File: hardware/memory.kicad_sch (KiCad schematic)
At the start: 5 parts, among them U2 ICE40HX4K-TQ144

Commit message: Add 3d models, re-place exp slots, add components
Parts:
- added U3, U4: SN74ALVC164245, Package_SO:TSSOP-48_6.1x12.5mm_P0.5mm, symbol 68040:SN74ALVC164245
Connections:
- net D0: now also U3.2 (1B1); no longer J10.2 (DQ0), J11.2 (DQ0), J12.2 (DQ0), J9.2 (DQ0)
- net D1: now also U3.3 (1B2); no longer J10.4 (DQ1), J11.4 (DQ1), J12.4 (DQ1), J9.4 (DQ1)
- net D10: now also U3.16 (2B3); no longer J10.53 (DQ10), J11.53 (DQ10), J12.53 (DQ10), J9.53 (DQ10)
- net D11: now also U3.17 (2B4); no longer J10.55 (DQ11), J11.55 (DQ11), J12.55 (DQ11), J9.55 (DQ11)
- net D12: now also U3.19 (2B5); no longer J10.57 (DQ12), J11.57 (DQ12), J12.57 (DQ12), J9.57 (DQ12)
- net D13: now also U3.20 (2B6); no longer J10.61 (DQ13), J11.61 (DQ13), J12.61 (DQ13), J9.61 (DQ13)
- net D14: now also U3.22 (2B7); no longer J10.63 (DQ14), J11.63 (DQ14), J12.63 (DQ14), J9.63 (DQ14)
- net D15: now also U3.23 (2B8); no longer J10.65 (DQ15), J11.65 (DQ15), J12.65 (DQ15), J9.65 (DQ15)
- net D16: now also U4.2 (1B1); no longer J10.3 (DQ16), J11.3 (DQ16), J12.3 (DQ16), J9.3 (DQ16)
- net D17: now also U4.3 (1B2); no longer J10.5 (DQ17), J11.5 (DQ17), J12.5 (DQ17), J9.5 (DQ17)
- net D18: now also U4.5 (1B3); no longer J10.7 (DQ18), J11.7 (DQ18), J12.7 (DQ18), J9.7 (DQ18)
- net D19: now also U4.6 (1B4); no longer J10.9 (DQ19), J11.9 (DQ19), J12.9 (DQ19), J9.9 (DQ19)
- net D2: now also U3.5 (1B3); no longer J10.6 (DQ2), J11.6 (DQ2), J12.6 (DQ2), J9.6 (DQ2)
- net D20: now also U4.8 (1B5); no longer J10.21 (DQ20), J11.21 (DQ20), J12.21 (DQ20), J9.21 (DQ20)
- net D21: now also U4.9 (1B6); no longer J10.23 (DQ21), J11.23 (DQ21), J12.23 (DQ21), J9.23 (DQ21)
- net D22: now also U4.11 (1B7); no longer J10.25 (DQ22), J11.25 (DQ22), J12.25 (DQ22), J9.25 (DQ22)
- net D23: now also U4.12 (1B8); no longer J10.27 (DQ23), J11.27 (DQ23), J12.27 (DQ23), J9.27 (DQ23)
- net D24: now also U4.13 (2B1); no longer J10.50 (DQ24), J11.50 (DQ24), J12.50 (DQ24), J9.50 (DQ24)
- net D25: now also U4.14 (2B2); no longer J10.52 (DQ25), J11.52 (DQ25), J12.52 (DQ25), J9.52 (DQ25)
- net D26: now also U4.16 (2B3); no longer J10.54 (DQ26), J11.54 (DQ26), J12.54 (DQ26), J9.54 (DQ26)
- net D27: now also U4.17 (2B4); no longer J10.56 (DQ27), J11.56 (DQ27), J12.56 (DQ27), J9.56 (DQ27)
- net D28: now also U4.19 (2B5); no longer J10.58 (DQ28), J11.58 (DQ28), J12.58 (DQ28), J9.58 (DQ28)
- net D29: now also U4.20 (2B6); no longer J10.60 (DQ29), J11.60 (DQ29), J12.60 (DQ29), J9.60 (DQ29)
- net D3: now also U3.6 (1B4); no longer J10.8 (DQ3), J11.8 (DQ3), J12.8 (DQ3), J9.8 (DQ3)
- net D30: now also U4.22 (2B7); no longer J10.62 (DQ30), J11.62 (DQ30), J12.62 (DQ30), J9.62 (DQ30)
- net D31: now also U4.23 (2B8); no longer J10.64 (DQ31), J11.64 (DQ31), J12.64 (DQ31), J9.64 (DQ31)
- net D4: now also U3.8 (1B5); no longer J10.20 (DQ4), J11.20 (DQ4), J12.20 (DQ4), J9.20 (DQ4)
- net D5: now also U3.9 (1B6); no longer J10.22 (DQ5), J11.22 (DQ5), J12.22 (DQ5), J9.22 (DQ5)
- net D6: now also U3.11 (1B7); no longer J10.24 (DQ6), J11.24 (DQ6), J12.24 (DQ6), J9.24 (DQ6)
- net D7: now also U3.12 (1B8); no longer J10.26 (DQ7), J11.26 (DQ7), J12.26 (DQ7), J9.26 (DQ7)
- net D8: now also U3.13 (2B1); no longer J10.49 (DQ8), J11.49 (DQ8), J12.49 (DQ8), J9.49 (DQ8)
- net D9: now also U3.14 (2B2); no longer J10.51 (DQ9), J11.51 (DQ9), J12.51 (DQ9), J9.51 (DQ9)
- new net DRAM_D0: J10.2 (DQ0), J11.2 (DQ0), J12.2 (DQ0), J9.2 (DQ0), U3.47 (1A1)
- new net DRAM_D1: J10.4 (DQ1), J11.4 (DQ1), J12.4 (DQ1), J9.4 (DQ1), U3.46 (1A2)
- new net DRAM_D10: J10.53 (DQ10), J11.53 (DQ10), J12.53 (DQ10), J9.53 (DQ10), U3.33 (2A3)
- new net DRAM_D11: J10.55 (DQ11), J11.55 (DQ11), J12.55 (DQ11), J9.55 (DQ11), U3.32 (2A4)
- new net DRAM_D12: J10.57 (DQ12), J11.57 (DQ12), J12.57 (DQ12), J9.57 (DQ12), U3.30 (2A5)
- new net DRAM_D13: J10.61 (DQ13), J11.61 (DQ13), J12.61 (DQ13), J9.61 (DQ13), U3.29 (2A6)
- new net DRAM_D14: J10.63 (DQ14), J11.63 (DQ14), J12.63 (DQ14), J9.63 (DQ14), U3.27 (2A7)
- new net DRAM_D15: J10.65 (DQ15), J11.65 (DQ15), J12.65 (DQ15), J9.65 (DQ15), U3.26 (2A8)
- new net DRAM_D16: J10.3 (DQ16), J11.3 (DQ16), J12.3 (DQ16), J9.3 (DQ16), U4.47 (1A1)
- new net DRAM_D17: J10.5 (DQ17), J11.5 (DQ17), J12.5 (DQ17), J9.5 (DQ17), U4.46 (1A2)
- new net DRAM_D18: J10.7 (DQ18), J11.7 (DQ18), J12.7 (DQ18), J9.7 (DQ18), U4.44 (1A3)
- new net DRAM_D19: J10.9 (DQ19), J11.9 (DQ19), J12.9 (DQ19), J9.9 (DQ19), U4.43 (1A4)
- new net DRAM_D2: J10.6 (DQ2), J11.6 (DQ2), J12.6 (DQ2), J9.6 (DQ2), U3.44 (1A3)
- new net DRAM_D20: J10.21 (DQ20), J11.21 (DQ20), J12.21 (DQ20), J9.21 (DQ20), U4.41 (1A5)
- new net DRAM_D21: J10.23 (DQ21), J11.23 (DQ21), J12.23 (DQ21), J9.23 (DQ21), U4.40 (1A6)
- new net DRAM_D22: J10.25 (DQ22), J11.25 (DQ22), J12.25 (DQ22), J9.25 (DQ22), U4.38 (1A7)
- new net DRAM_D23: J10.27 (DQ23), J11.27 (DQ23), J12.27 (DQ23), J9.27 (DQ23), U4.37 (1A8)
- new net DRAM_D24: J10.50 (DQ24), J11.50 (DQ24), J12.50 (DQ24), J9.50 (DQ24), U4.36 (2A1)
- new net DRAM_D25: J10.52 (DQ25), J11.52 (DQ25), J12.52 (DQ25), J9.52 (DQ25), U4.35 (2A2)
- new net DRAM_D26: J10.54 (DQ26), J11.54 (DQ26), J12.54 (DQ26), J9.54 (DQ26), U4.33 (2A3)
- new net DRAM_D27: J10.56 (DQ27), J11.56 (DQ27), J12.56 (DQ27), J9.56 (DQ27), U4.32 (2A4)
- new net DRAM_D28: J10.58 (DQ28), J11.58 (DQ28), J12.58 (DQ28), J9.58 (DQ28), U4.30 (2A5)
- new net DRAM_D29: J10.60 (DQ29), J11.60 (DQ29), J12.60 (DQ29), J9.60 (DQ29), U4.29 (2A6)
- new net DRAM_D3: J10.8 (DQ3), J11.8 (DQ3), J12.8 (DQ3), J9.8 (DQ3), U3.43 (1A4)
- new net DRAM_D30: J10.62 (DQ30), J11.62 (DQ30), J12.62 (DQ30), J9.62 (DQ30), U4.27 (2A7)
- new net DRAM_D31: J10.64 (DQ31), J11.64 (DQ31), J12.64 (DQ31), J9.64 (DQ31), U4.26 (2A8)
- new net DRAM_D4: J10.20 (DQ4), J11.20 (DQ4), J12.20 (DQ4), J9.20 (DQ4), U3.41 (1A5)
- new net DRAM_D5: J10.22 (DQ5), J11.22 (DQ5), J12.22 (DQ5), J9.22 (DQ5), U3.40 (1A6)
- new net DRAM_D6: J10.24 (DQ6), J11.24 (DQ6), J12.24 (DQ6), J9.24 (DQ6), U3.38 (1A7)
- new net DRAM_D7: J10.26 (DQ7), J11.26 (DQ7), J12.26 (DQ7), J9.26 (DQ7), U3.37 (1A8)
- new net DRAM_D8: J10.49 (DQ8), J11.49 (DQ8), J12.49 (DQ8), J9.49 (DQ8), U3.36 (2A1)
- new net DRAM_D9: J10.51 (DQ9), J11.51 (DQ9), J12.51 (DQ9), J9.51 (DQ9), U3.35 (2A2)
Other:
- moved on the sheet: J10, J11, J12, J9, U2A, U2B, U2C, U2D, U2E

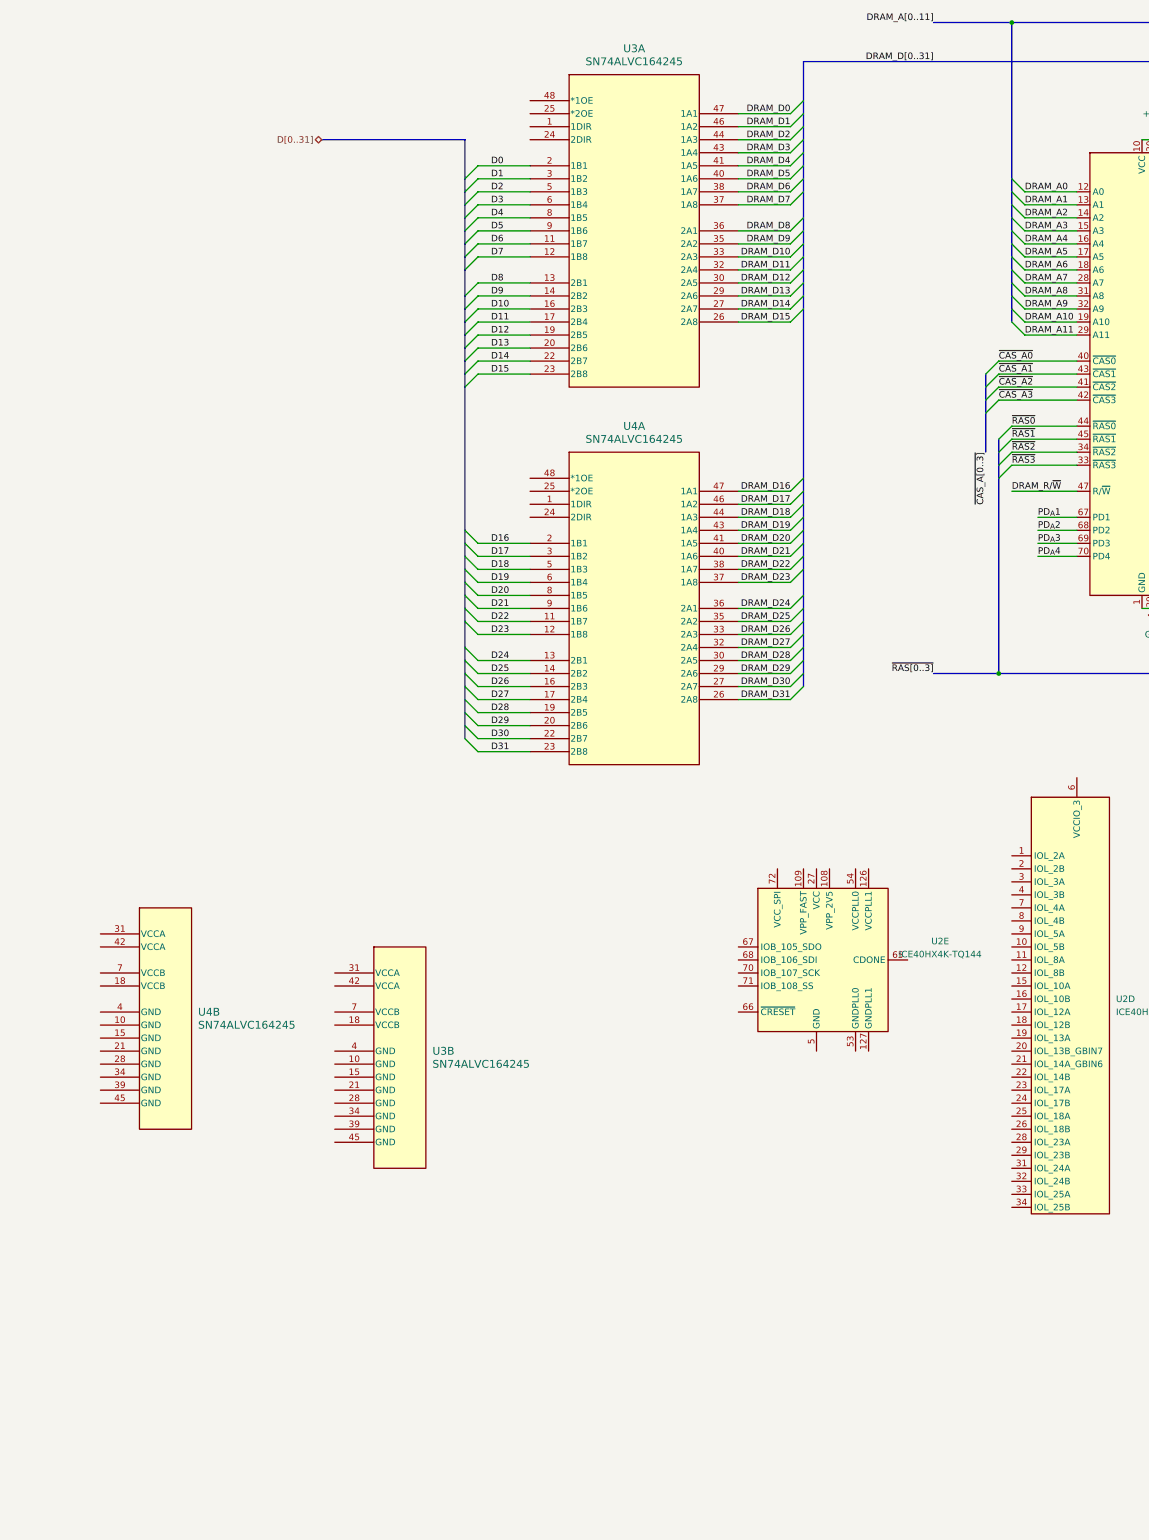
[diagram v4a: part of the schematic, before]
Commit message: reconfigure expansion slot schematic
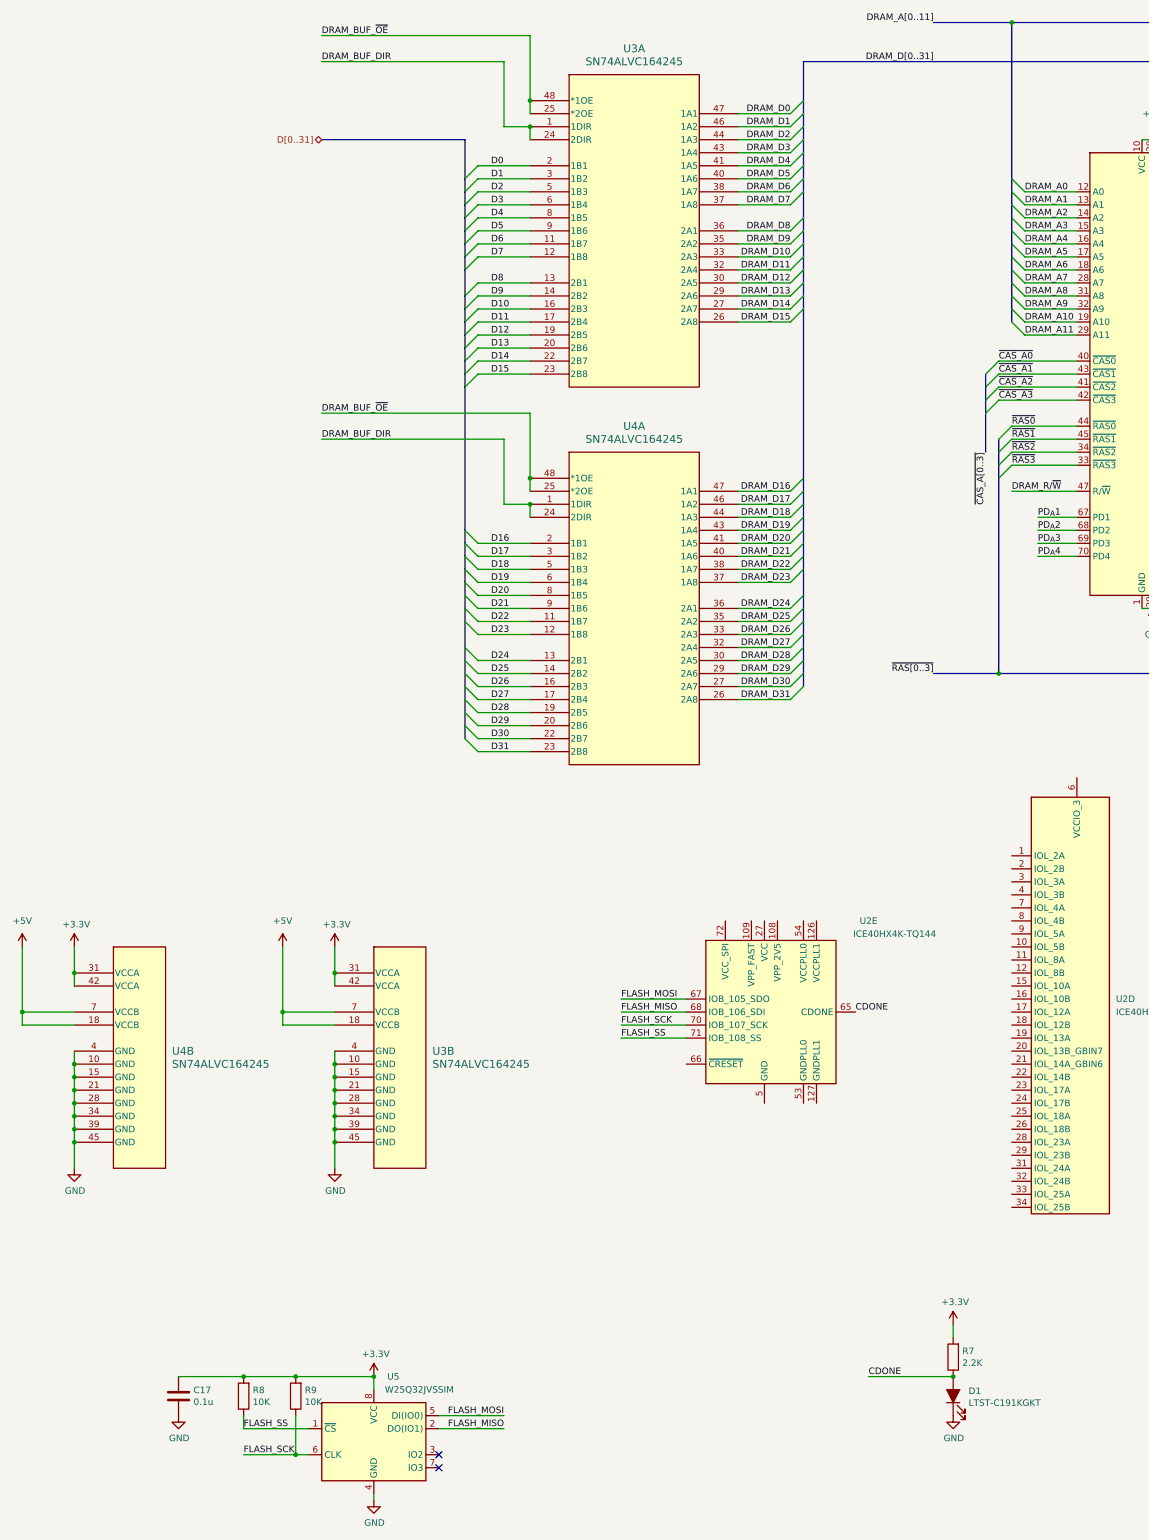
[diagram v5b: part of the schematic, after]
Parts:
- added C17: 0.1u, Capacitor_SMD:C_0603_1608Metric, symbol UPduino_v3.0:Device_C
- added D1: LTST-C191KGKT, LED_SMD:LED_0603_1608Metric, symbol UPduino_v3.0:Device_LED_ALT
- added R7: 2.2K, Resistor_SMD:R_0603_1608Metric, symbol UPduino_v3.0:Device_R
- added R8, R9: 10K, Resistor_SMD:R_0603_1608Metric, symbol UPduino_v3.0:Device_R
- added U5: W25Q32JVSSIM, Package_SO:SOIC-8_5.23x5.23mm_P1.27mm, symbol UPduino_v3.0:W25Q32JVSS-Memory_Flash
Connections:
- net +3V3: now also U3.31 (VCCA), U3.42 (VCCA), U4.31 (VCCA), U4.42 (VCCA), C17.1, R7.2, R8.2, R9.2, U5.8 (VCC)
- net GND: now also U3.10 (GND), U3.15 (GND), U3.21 (GND), U3.28 (GND), U3.34 (GND), U3.39 (GND), U3.4 (GND), U3.45 (GND), U4.10 (GND), U4.15 (GND), U4.21 (GND), U4.28 (GND), U4.34 (GND), U4.39 (GND), U4.4 (GND), U4.45 (GND), C17.2, D1.1 (K), U5.4 (GND)
- net DRAM_BUF_DIR: now reaches U4.1 (1DIR)
- net DRAM_BUF_DIR: now also U3.1 (1DIR), U3.24 (2DIR), U4.24 (2DIR)
- net DRAM_BUF_~{OE}: now reaches U4.25 (*2OE)
- net DRAM_BUF_~{OE}: now also U3.25 (*2OE), U3.48 (*1OE), U4.48 (*1OE)
- net CDONE: now reaches U2.65 (CDONE)
- net CDONE: now also D1.2 (A), R7.1
- net FLASH_MOSI: now reaches U2.67 (IOB_105_SDO)
- net FLASH_MOSI: now also U5.5 (DI(IO0))
- net FLASH_MISO: now reaches U2.68 (IOB_106_SDI)
- net FLASH_MISO: now also U5.2 (DO(IO1))
- net FLASH_SCK: now reaches U2.70 (IOB_107_SCK)
- net FLASH_SCK: now also R9.1, U5.6 (CLK)
- net FLASH_SS: now reaches U2.71 (IOB_108_SS)
- net FLASH_SS: now also R8.1, U5.1 (~{CS})
- net +5V: now reaches U3.18 (VCCB)
- net +5V: now also U3.7 (VCCB), U4.18 (VCCB), U4.7 (VCCB)
- no-connect marks 0 -> 2
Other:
- moved on the sheet: U2E, U4B

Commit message: updates
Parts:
- added RN3, RN4, RN5, RN6: 10k, Resistor_THT:R_Array_SIP5, symbol Device:R_Network04_US
- added U10, U9: 74HC165, Package_SO:SOIC-16_3.9x9.9mm_P1.27mm, symbol 74xx:74HC165
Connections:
- net +3V3: now also RN3.1 (common), RN4.1 (common), RN5.1 (common), U10.16 (VCC), U9.16 (VCC)
- net GND: now also U10.15 (~{CE}), U10.8 (GND), U9.10 (DS), U9.15 (~{CE}), U9.8 (GND)
- net PD_{A}1: now also RN5.2 (R1), U9.11 (D0)
- net PD_{A}2: now also RN5.3 (R2), U9.12 (D1)
- net PD_{A}3: now also RN5.4 (R3), U9.13 (D2)
- net PD_{A}4: now also RN5.5 (R4), U9.14 (D3)
- net PD_{B}1: now also RN6.2 (R1), U9.3 (D4)
- net PD_{B}2: now also RN6.3 (R2), U9.4 (D5)
- net PD_{B}3: now also RN6.4 (R3), U9.5 (D6)
- net PD_{B}4: now also RN6.5 (R4), U9.6 (D7)
- net PD_{C}1: now also RN3.2 (R1), U10.11 (D0)
- net PD_{C}2: now also RN3.3 (R2), U10.12 (D1)
- net PD_{C}3: now also RN3.4 (R3), U10.13 (D2)
- net PD_{C}4: now also RN3.5 (R4), U10.14 (D3)
- net PD_{D}1: now also RN4.2 (R1), U10.3 (D4)
- net PD_{D}2: now also RN4.3 (R2), U10.4 (D5)
- net PD_{D}3: now also RN4.4 (R3), U10.5 (D6)
- net PD_{D}4: now also RN4.5 (R4), U10.6 (D7)
- new net: U10.10 (DS), U9.9 (Q7)
- new net RAMPDSR_CLK: U10.2 (CP), U9.2 (CP)
- new net RAMPDSR_D_{OUT}: U10.9 (Q7)
- new net RAMPDSR_SH/~{LD}: U10.1 (~{PL}), U9.1 (~{PL})
- no-connect marks 2 -> 4
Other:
- note added: "Presence detect circuitry Should probably be HCT"

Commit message: updates
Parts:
- added U15, U16, U17, U18: SN74ALVC164245, Package_SO:TSSOP-48_6.1x12.5mm_P0.5mm, symbol 68040:SN74ALVC164245
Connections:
- net A0: now also U15.2 (1B1); no longer U2.88 (IOR_137)
- net A1: now also U15.3 (1B2); no longer U2.90 (IOR_138)
- net A10: now also U15.16 (2B3); no longer U2.101 (IOR_160)
- net A11: now also U15.17 (2B4); no longer U2.102 (IOR_161)
- net A12: now also U15.19 (2B5); no longer U2.104 (IOR_164)
- net A13: now also U15.20 (2B6); no longer U2.105 (IOR_165)
- net A14: now also U15.22 (2B7); no longer U2.106 (IOR_166)
- net A15: now also U15.23 (2B8); no longer U2.107 (IOR_167)
- net A16: now also U16.23 (2B8); no longer U2.110 (IOT_168)
- net A17: now also U16.22 (2B7); no longer U2.112 (IOT_169)
- net A18: now also U16.20 (2B6); no longer U2.113 (IOT_170)
- net A19: now also U16.19 (2B5); no longer U2.114 (IOT_171)
- net A2: now also U15.5 (1B3); no longer U2.91 (IOR_139)
- net A20: now also U16.17 (2B4); no longer U2.115 (IOT_172)
- net A21: now also U16.16 (2B3); no longer U2.116 (IOT_173)
- net A22: now also U16.14 (2B2); no longer U2.117 (IOT_174)
- net A23: now also U16.13 (2B1); no longer U2.118 (IOT_177)
- net A24: now also U16.12 (1B8); no longer U2.119 (IOT_178)
- net A25: now also U16.11 (1B7); no longer U2.120 (IOT_179)
- net A26: now also U16.9 (1B6); no longer U2.121 (IOT_181)
- net A27: now also U16.8 (1B5); no longer U2.122 (IOT_190)
- net A28: now also U16.6 (1B4); no longer U2.124 (IOT_191)
- net A29: now also U16.5 (1B3); no longer U2.125 (IOT_192)
- net A3: now also U15.6 (1B4); no longer U2.93 (IOR_140_GBIN3)
- net A30: now also U16.3 (1B2); no longer U2.128 (IOT_197_GBIN1)
- net A31: now also U16.2 (1B1); no longer U2.129 (IOT_198_GBIN0)
- net A4: now also U15.8 (1B5); no longer U2.94 (IOR_141_GBIN2)
- net A5: now also U15.9 (1B6); no longer U2.95 (IOR_144)
- net A6: now also U15.11 (1B7); no longer U2.96 (IOR_146)
- net A7: now also U15.12 (1B8); no longer U2.97 (IOR_147)
- net A8: now also U15.13 (2B1); no longer U2.98 (IOR_148)
- net A9: now also U15.14 (2B2); no longer U2.99 (IOR_152)
- net D0: now also U17.2 (1B1)
- net D1: now also U17.3 (1B2)
- net D10: now also U17.16 (2B3)
- net D11: now also U17.17 (2B4)
- net D12: now also U17.19 (2B5)
- net D13: now also U17.20 (2B6)
- net D14: now also U17.22 (2B7)
- net D15: now also U17.23 (2B8)
- net D16: now also U18.2 (1B1)
- net D17: now also U18.3 (1B2)
- net D18: now also U18.5 (1B3)
- net D19: now also U18.6 (1B4)
- net D2: now also U17.5 (1B3)
- net D20: now also U18.8 (1B5)
- net D21: now also U18.9 (1B6)
- net D22: now also U18.11 (1B7)
- net D23: now also U18.12 (1B8)
- net D24: now also U18.13 (2B1)
- net D25: now also U18.14 (2B2)
- net D26: now also U18.16 (2B3)
- net D27: now also U18.17 (2B4)
- net D28: now also U18.19 (2B5)
- net D29: now also U18.20 (2B6)
- net D3: now also U17.6 (1B4)
- net D30: now also U18.22 (2B7)
- net D31: now also U18.23 (2B8)
- net D4: now also U17.8 (1B5)
- net D5: now also U17.9 (1B6)
- net D6: now also U17.11 (1B7)
- net D7: now also U17.12 (1B8)
- net D8: now also U17.13 (2B1)
- net D9: now also U17.14 (2B2)
- net FPGA_D24: now reaches U2.1 (IOL_2A)
- net FPGA_D24: now also U18.36 (2A1)
- net FPGA_D31: now reaches U2.10 (IOL_5B)
- net FPGA_D31: now also U18.26 (2A8)
- net FPGA_D25: now reaches U2.2 (IOL_2B)
- net FPGA_D25: now also U18.35 (2A2)
- net FPGA_D26: now reaches U2.3 (IOL_3A)
- net FPGA_D26: now also U18.33 (2A3)
- net FPGA_D27: now reaches U2.4 (IOL_3B)
- net FPGA_D27: now also U18.32 (2A4)
- net FPGA_D28: now reaches U2.7 (IOL_4A)
- net FPGA_D28: now also U18.30 (2A5)
- net FPGA_D29: now reaches U2.8 (IOL_4B)
- net FPGA_D29: now also U18.29 (2A6)
- net FPGA_D30: now reaches U2.9 (IOL_5A)
- net FPGA_D30: now also U18.27 (2A7)
- net FPGA_A0: now reaches U2.73 (IOR_109)
- net FPGA_A0: now also U15.47 (1A1)
- net FPGA_A1: now reaches U2.74 (IOR_110)
- net FPGA_A1: now also U15.46 (1A2)
- net FPGA_A2: now reaches U2.75 (IOR_111)
- net FPGA_A2: now also U15.44 (1A3)
- net FPGA_A3: now reaches U2.76 (IOR_112)
- net FPGA_A3: now also U15.43 (1A4)
- net FPGA_A4: now reaches U2.78 (IOR_114)
- net FPGA_A4: now also U15.41 (1A5)
- net FPGA_A5: now reaches U2.79 (IOR_115)
- net FPGA_A5: now also U15.40 (1A6)
- net FPGA_A6: now reaches U2.80 (IOR_116)
- net FPGA_A6: now also U15.38 (1A7)
- net FPGA_A7: now reaches U2.81 (IOR_117)
- net FPGA_A7: now also U15.37 (1A8)
- net FPGA_A8: now reaches U2.82 (IOR_118)
- net FPGA_A8: now also U15.36 (2A1)
- net FPGA_A9: now reaches U2.83 (IOR_119)
- net FPGA_A9: now also U15.35 (2A2)
- net FPGA_A10: now reaches U2.84 (IOR_120)
- net FPGA_A10: now also U15.33 (2A3)
- net FPGA_A11: now reaches U2.85 (IOR_128)
- net FPGA_A11: now also U15.32 (2A4)
- net FPGA_A12: now reaches U2.87 (IOR_136)
- net FPGA_A12: now also U15.30 (2A5)
- net FPGA_D13: now reaches U2.130 (IOT_206)
- net FPGA_D13: now also U17.29 (2A6)
- net FPGA_D14: now reaches U2.134 (IOT_212)
- net FPGA_D14: now also U17.27 (2A7)
- net FPGA_D15: now reaches U2.135 (IOT_213)
- net FPGA_D15: now also U17.26 (2A8)
- new net FPGA_A13: U15.29 (2A6), U2.88 (IOR_137)
- new net FPGA_A14: U15.27 (2A7), U2.90 (IOR_138)
- new net FPGA_A15: U15.26 (2A8), U2.91 (IOR_139)
- new net FPGA_A16: U16.26 (2A8), U2.110 (IOT_168)
- new net FPGA_A17: U16.27 (2A7), U2.112 (IOT_169)
- new net FPGA_A18: U16.29 (2A6), U2.113 (IOT_170)
- new net FPGA_A19: U16.30 (2A5), U2.107 (IOR_167)
- new net FPGA_A20: U16.32 (2A4), U2.106 (IOR_166)
- new net FPGA_A21: U16.33 (2A3), U2.105 (IOR_165)
- new net FPGA_A22: U16.35 (2A2), U2.104 (IOR_164)
- new net FPGA_A23: U16.36 (2A1), U2.102 (IOR_161)
- new net FPGA_A24: U16.37 (1A8), U2.101 (IOR_160)
- new net FPGA_A25: U16.38 (1A7), U2.99 (IOR_152)
- new net FPGA_A26: U16.40 (1A6), U2.98 (IOR_148)
- new net FPGA_A27: U16.41 (1A5), U2.97 (IOR_147)
- new net FPGA_A28: U16.43 (1A4), U2.96 (IOR_146)
- new net FPGA_A29: U16.44 (1A3), U2.95 (IOR_144)
- new net FPGA_A30: U16.46 (1A2), U2.94 (IOR_141_GBIN2)
- new net FPGA_A31: U16.47 (1A1), U2.93 (IOR_140_GBIN3)
- new net FPGA_D0: U17.47 (1A1), U2.114 (IOT_171)
- new net FPGA_D1: U17.46 (1A2), U2.115 (IOT_172)
- new net FPGA_D10: U17.33 (2A3), U2.125 (IOT_192)
- new net FPGA_D11: U17.32 (2A4), U2.128 (IOT_197_GBIN1)
- new net FPGA_D12: U17.30 (2A5), U2.129 (IOT_198_GBIN0)
- new net FPGA_D16: U18.47 (1A1)
- new net FPGA_D17: U18.46 (1A2)
- new net FPGA_D18: U18.44 (1A3)
- new net FPGA_D19: U18.43 (1A4)
- new net FPGA_D2: U17.44 (1A3), U2.116 (IOT_173)
- new net FPGA_D20: U18.41 (1A5)
- new net FPGA_D21: U18.40 (1A6)
- new net FPGA_D22: U18.38 (1A7)
- new net FPGA_D23: U18.37 (1A8)
- new net FPGA_D3: U17.43 (1A4), U2.117 (IOT_174)
- new net FPGA_D4: U17.41 (1A5), U2.118 (IOT_177)
- new net FPGA_D5: U17.40 (1A6), U2.119 (IOT_178)
- new net FPGA_D6: U17.38 (1A7), U2.120 (IOT_179)
- new net FPGA_D7: U17.37 (1A8), U2.121 (IOT_181)
- new net FPGA_D8: U17.36 (2A1), U2.122 (IOT_190)
- new net FPGA_D9: U17.35 (2A2), U2.124 (IOT_191)
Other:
- moved on the sheet: U2A
